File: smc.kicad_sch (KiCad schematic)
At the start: 42 parts, among them SW1 SW_Push, SW2 SW_Push, U5 W25Q128JVS, U6 RP2040, Y1 12MHz 20pF

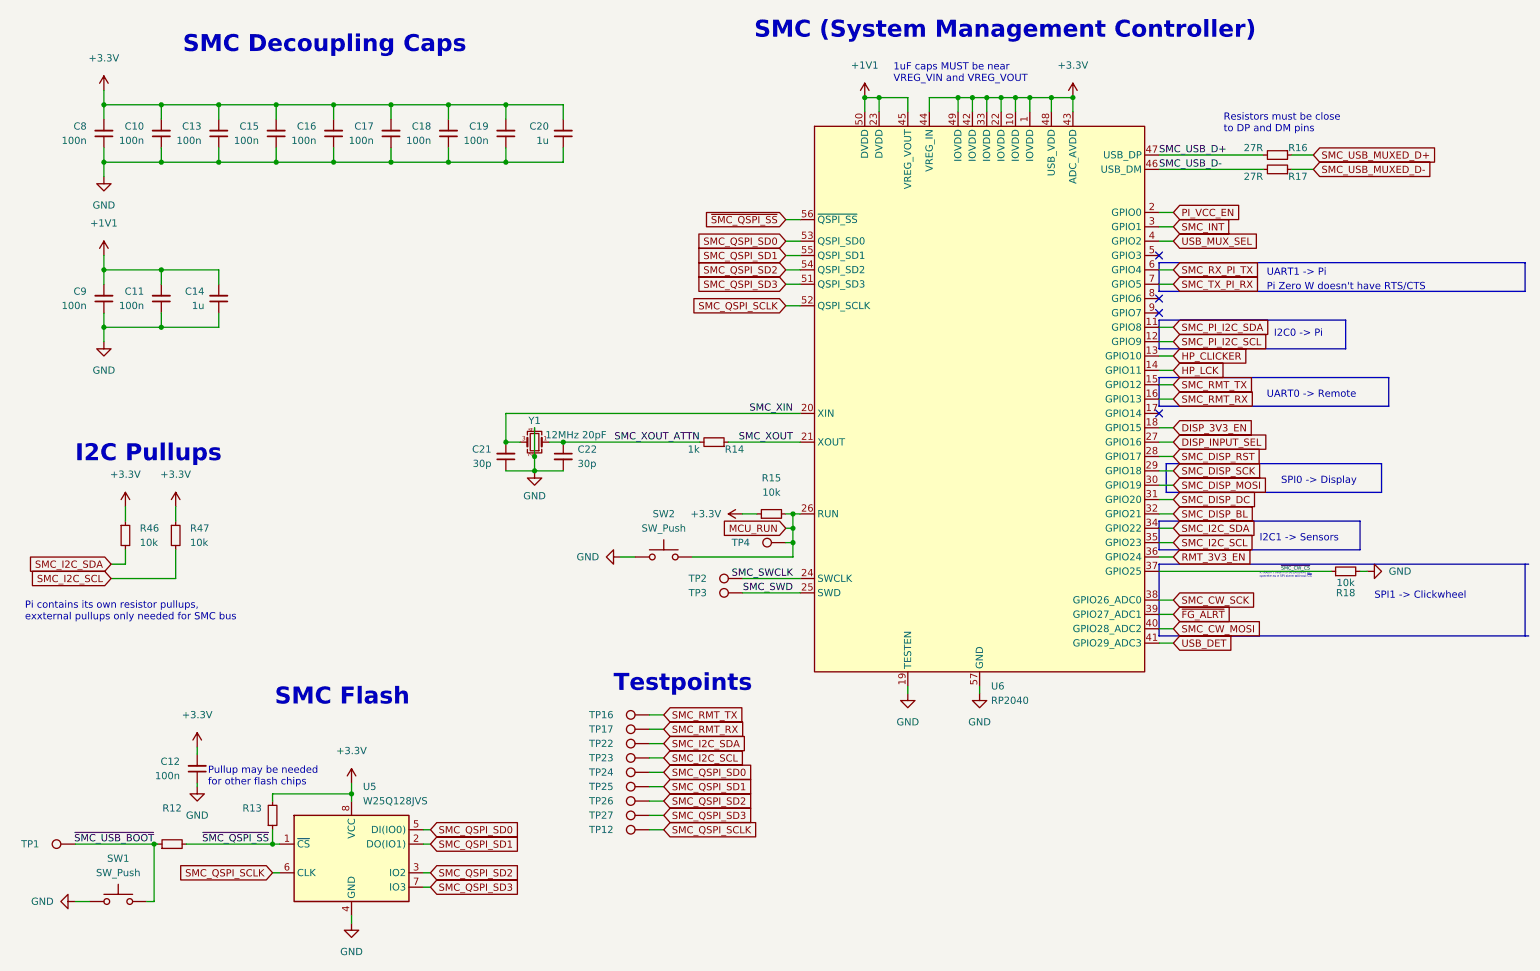
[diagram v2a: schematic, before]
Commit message: schematic: add resistors to allow latching pi power
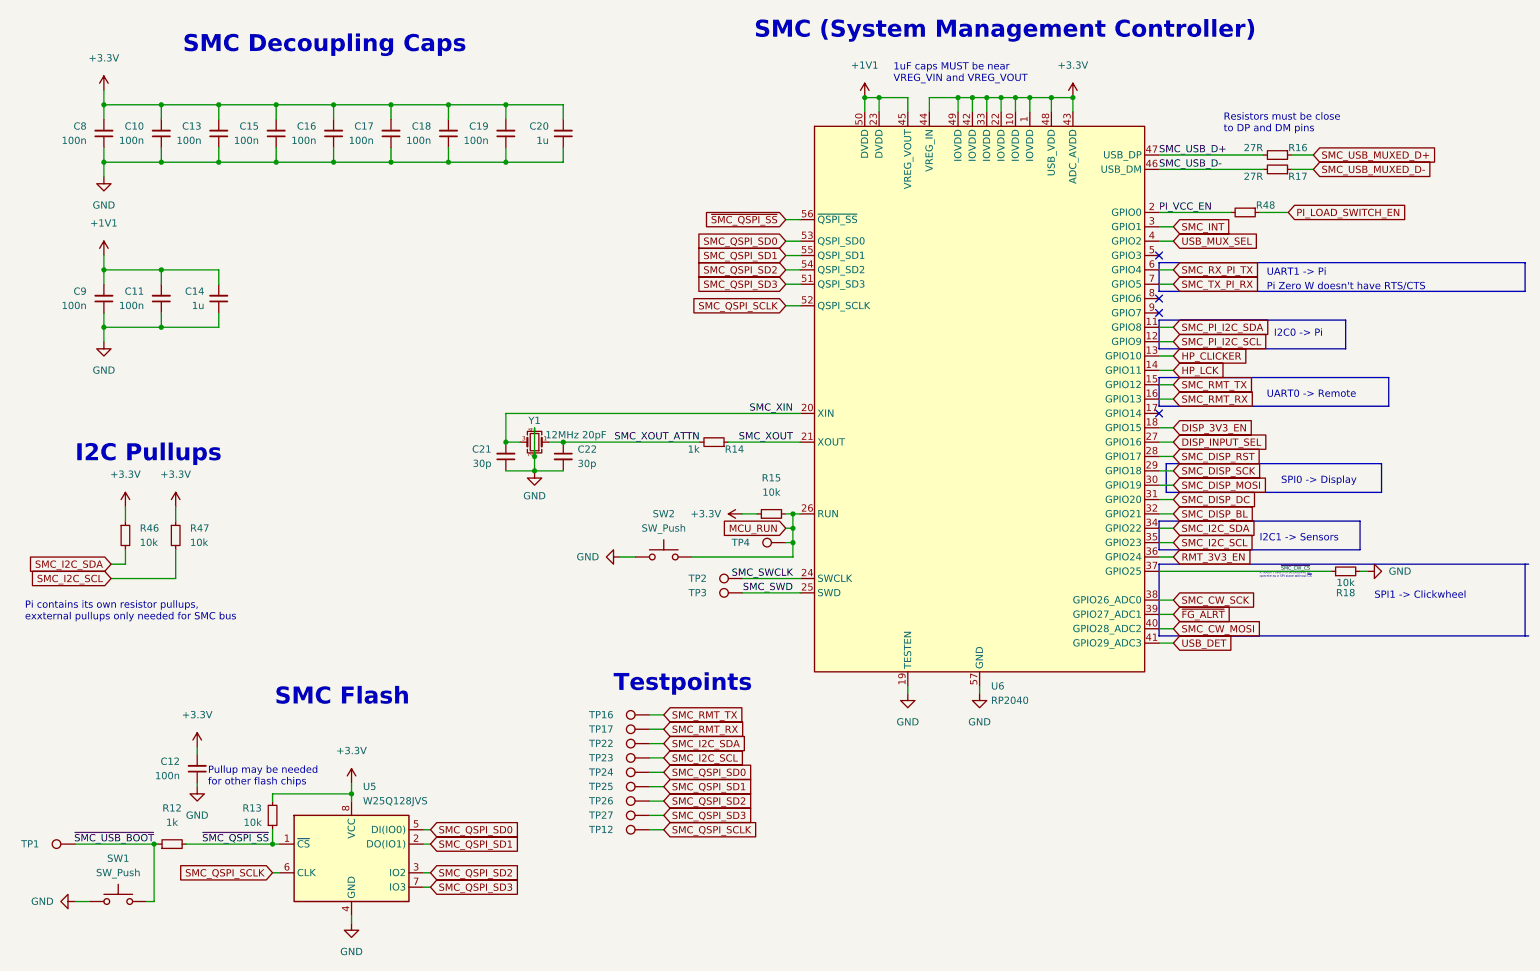
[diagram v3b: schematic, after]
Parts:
- added R48: (no value), symbol Device:R_Small
- R12: value (none) -> 1k
- R13: value (none) -> 10k
- SW1, SW2: footprint (none) -> Gigahawk:SW_Push_1P1T_NO_CK_KMR2
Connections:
- net PI_VCC_EN: now also R48.2
- new net PI_LOAD_SWITCH_EN: R48.1
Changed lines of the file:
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@@
     (stroke (width 0) (type default) (color 0 0 0 0))
   )
-  (wire (pts (xy 217.17 63.5) (xy 219.71 63.5))
+  (wire (pts (xy 217.17 63.5) (xy 229.87 63.5))
     (stroke (width 0) (type default) (color 0 0 0 0))
   )
@@
   )
   (wire (pts (xy 217.17 76.2) (xy 219.71 76.2))
+    (stroke (width 0) (type default) (color 0 0 0 0))
+  )
+  (wire (pts (xy 234.95 63.5) (xy 240.03 63.5))
     (stroke (width 0) (type default) (color 0 0 0 0))
   )
@@
   (label "~{SMC_QSPI_SS}" (at 59.69 175.26 180)
     (effects (font (size 1.27 1.27)) (justify right bottom))
+  )
+  (label "PI_VCC_EN" (at 217.17 63.5 0)
+    (effects (font (size 1.27 1.27)) (justify left bottom))
   )
   (label "~{SMC_CW_CS}" (at 238.76 127 0)
@@
     )
   )
+  (global_label "PI_LOAD_SWITCH_EN" (shape input) (at 240.03 63.5 0) (fields_autoplaced)
+    (effects (font (size 1.27 1.27)) (justify left))
+    (property "Intersheet References" "${INTERSHEET_REFS}" (id 0) (at 261.2512 63.4206 0)
+      (effects (font (size 1.27 1.27)) (justify left) hide)
+    )
+  )
   (global_label "SMC_QSPI_SD1" (shape input) (at 129.54 165.1 0) (fields_autoplaced)
     (effects (font (size 1.27 1.27)) (justify left))
@@
     )
   )
-  (global_label "PI_VCC_EN" (shape input) (at 219.71 63.5 0) (fields_autoplaced)
-    (effects (font (size 1.27 1.27)) (justify left))
-    (property "Intersheet References" "${INTERSHEET_REFS}" (id 0) (at 231.9202 63.5794 0)
-      (effects (font (size 1.27 1.27)) (justify left) hide)
-    )
-  )
   (global_label "SMC_TX_PI_RX" (shape input) (at 219.71 76.2 0) (fields_autoplaced)
     (effects (font (size 1.27 1.27)) (justify left))
@@
     (in_bom yes) (on_board yes) (fields_autoplaced)
     (property "Reference" "R12" (id 0) (at 42.545 168.91 90))
-    (property "Value" "" (id 1) (at 42.545 171.45 90))
+    (property "Value" "1k" (id 1) (at 42.545 171.45 90))
     (property "Footprint" "Resistor_SMD:R_0402_1005Metric" (id 2) (at 42.545 175.26 0)
       (effects (font (size 1.27 1.27)) hide)
@@
       (effects (font (size 1.27 1.27)) (justify right))
     )
-    (property "Value" "" (id 1) (at 58.42 171.4499 0)
+    (property "Value" "10k" (id 1) (at 58.42 171.4499 0)
       (effects (font (size 1.27 1.27)) (justify right))
     )
@@
     )
     (pin "1")
+  )
+  (symbol (lib_id "Device:R_Small") (at 232.41 63.5 270) (unit 1)
+    (in_bom yes) (on_board yes)
+    (property "Reference" "R48" (id 0) (at 234.315 62.23 90)
+      (effects (font (size 1.27 1.27)) (justify left))
+    )
+    (property "Value" "" (id 1) (at 229.87 62.23 90)
+      (effects (font (size 1.27 1.27)) (justify right))
+    )
+    (property "Footprint" "" (id 2) (at 232.41 63.5 0)
+      (effects (font (size 1.27 1.27)) hide)
+    )
+    (property "Datasheet" "~" (id 3) (at 232.41 63.5 0)
+      (effects (font (size 1.27 1.27)) hide)
+    )
+    (pin "1")
+    (pin "2")
   )
   (symbol (lib_id "Device:R_Small") (at 43.18 120.65 0) (unit 1)
@@
     (property "Reference" "SW1" (id 0) (at 33.02 177.8 0))
     (property "Value" "SW_Push" (id 1) (at 33.02 180.34 0))
-    (property "Footprint" "" (id 2) (at 33.02 180.34 0)
+    (property "Footprint" "Gigahawk:SW_Push_1P1T_NO_CK_KMR2" (id 2) (at 33.02 180.34 0)
       (effects (font (size 1.27 1.27)) hide)
     )
@@
     (property "Reference" "SW2" (id 0) (at 129.54 116.84 0))
     (property "Value" "SW_Push" (id 1) (at 129.54 119.38 0))
-    (property "Footprint" "" (id 2) (at 129.54 119.38 0)
-      (effects (font (size 1.27 1.27)) hide)
-    )
+    (property "Footprint" "Gigahawk:SW_Push_1P1T_NO_CK_KMR2" (id 2) (at 129.54 119.38 0)
+      (effects (font (size 1.27 1.27)) hide)
+    )

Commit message: compute: finish layout and routing
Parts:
- added D4: (no value), symbol Device:LED
- added R50: (no value), symbol Device:R
- added TP34: TestPoint, TestPoint:TestPoint_Pad_D1.5mm, symbol Connector:TestPoint
- R48: value (none) -> 1k; footprint (none) -> Resistor_SMD:R_0402_1005Metric
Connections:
- net GND: now also R50.2
- net SMC_RX_PI_TX: now also U6.7 (GPIO5); no longer U6.6 (GPIO4)
- net SMC_TX_PI_RX: now also U6.6 (GPIO4); no longer U6.7 (GPIO5)
- net SMC_LED: now reaches U6.5 (GPIO3)
- net SMC_LED: now also D4.2 (A), TP34.1
- new net: D4.1 (K), R50.1
- no-connect marks 4 -> 3
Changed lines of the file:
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@@
   (no_connect (at 217.17 81.28))
   (no_connect (at 217.17 78.74))
-  (no_connect (at 217.17 71.12))
   (wire (pts (xy 217.17 93.98) (xy 219.71 93.98))
     (stroke (width 0) (type default) (color 0 0 0 0))
@@
     (stroke (width 0) (type default) (color 0 0 0 0))
   )
+  (wire (pts (xy 217.17 71.12) (xy 219.71 71.12))
+    (stroke (width 0) (type default) (color 0 0 0 0))
+  )
   (wire (pts (xy 217.17 116.84) (xy 219.71 116.84))
     (stroke (width 0) (type default) (color 0 0 0 0))
@@
     (stroke (width 0) (type default) (color 0 0 0 0))
   )
+  (wire (pts (xy 127 175.26) (xy 129.54 175.26))
+    (stroke (width 0) (type default) (color 0 0 0 0))
+  )
   (polyline (pts (xy 217.17 82.55) (xy 250.19 82.55))
     (stroke (width 0) (type default) (color 0 0 0 0))
@@
     (stroke (width 0) (type default) (color 0 0 0 0))
   )
+  (wire (pts (xy 119.38 74.93) (xy 119.38 77.47))
+    (stroke (width 0) (type default) (color 0 0 0 0))
+  )
   (wire (pts (xy 121.92 124.46) (xy 124.46 124.46))
     (stroke (width 0) (type default) (color 0 0 0 0))
@@
     (stroke (width 0) (type default) (color 0 0 0 0))
   )
+  (wire (pts (xy 119.38 64.77) (xy 119.38 67.31))
+    (stroke (width 0) (type default) (color 0 0 0 0))
+  )
   (wire (pts (xy 134.62 124.46) (xy 152.4 124.46))
     (stroke (width 0) (type default) (color 0 0 0 0))
@@
   )
   (wire (pts (xy 186.69 43.18) (xy 186.69 45.72))
+    (stroke (width 0) (type default) (color 0 0 0 0))
+  )
+  (wire (pts (xy 119.38 85.09) (xy 119.38 87.63))
     (stroke (width 0) (type default) (color 0 0 0 0))
   )
@@
     )
   )
+  (global_label "SMC_LED" (shape input) (at 129.54 175.26 0) (fields_autoplaced)
+    (effects (font (size 1.27 1.27)) (justify left))
+    (property "Intersheet References" "${INTERSHEET_REFS}" (id 0) (at 140.2988 175.1806 0)
+      (effects (font (size 1.27 1.27)) (justify left) hide)
+    )
+  )
   (global_label "~{FG_ALRT}" (shape input) (at 219.71 134.62 0) (fields_autoplaced)
     (effects (font (size 1.27 1.27)) (justify left))
@@
     )
   )
+  (global_label "SMC_LED" (shape input) (at 119.38 64.77 0) (fields_autoplaced)
+    (effects (font (size 1.27 1.27)) (justify left))
+    (property "Intersheet References" "${INTERSHEET_REFS}" (id 0) (at 130.1388 64.6906 0)
+      (effects (font (size 1.27 1.27)) (justify left) hide)
+    )
+  )
   (global_label "SMC_QSPI_SD2" (shape input) (at 129.54 167.64 0) (fields_autoplaced)
     (effects (font (size 1.27 1.27)) (justify left))
@@
     )
   )
+  (global_label "SMC_LED" (shape input) (at 219.71 71.12 0) (fields_autoplaced)
+    (effects (font (size 1.27 1.27)) (justify left))
+    (property "Intersheet References" "${INTERSHEET_REFS}" (id 0) (at 230.4688 71.0406 0)
+      (effects (font (size 1.27 1.27)) (justify left) hide)
+    )
+  )
   (global_label "HP_CLICKER" (shape input) (at 219.71 88.9 0) (fields_autoplaced)
     (effects (font (size 1.27 1.27)) (justify left))
@@
     )
   )
-  (global_label "SMC_RX_PI_TX" (shape input) (at 219.71 73.66 0) (fields_autoplaced)
-    (effects (font (size 1.27 1.27)) (justify left))
-    (property "Intersheet References" "${INTERSHEET_REFS}" (id 0) (at 235.4883 73.5806 0)
+  (global_label "SMC_RX_PI_TX" (shape input) (at 219.71 76.2 0) (fields_autoplaced)
+    (effects (font (size 1.27 1.27)) (justify left))
+    (property "Intersheet References" "${INTERSHEET_REFS}" (id 0) (at 235.4883 76.1206 0)
       (effects (font (size 1.27 1.27)) (justify left) hide)
     )
@@
     )
   )
-  (global_label "SMC_TX_PI_RX" (shape input) (at 219.71 76.2 0) (fields_autoplaced)
-    (effects (font (size 1.27 1.27)) (justify left))
-    (property "Intersheet References" "${INTERSHEET_REFS}" (id 0) (at 235.4883 76.1206 0)
+  (global_label "SMC_TX_PI_RX" (shape input) (at 219.71 73.66 0) (fields_autoplaced)
+    (effects (font (size 1.27 1.27)) (justify left))
+    (property "Intersheet References" "${INTERSHEET_REFS}" (id 0) (at 235.4883 73.5806 0)
       (effects (font (size 1.27 1.27)) (justify left) hide)
     )
@@
     (pin "2")
   )
+  (symbol (lib_id "Device:LED") (at 119.38 71.12 90) (unit 1)
+    (in_bom yes) (on_board yes) (fields_autoplaced)
+    (property "Reference" "D4" (id 0) (at 123.19 71.4374 90)
+      (effects (font (size 1.27 1.27)) (justify right))
+    )
+    (property "Value" "" (id 1) (at 123.19 73.9774 90)
+      (effects (font (size 1.27 1.27)) (justify right))
+    )
+    (property "Footprint" "" (id 2) (at 119.38 71.12 0)
+      (effects (font (size 1.27 1.27)) hide)
+    )
+    (property "Datasheet" "~" (id 3) (at 119.38 71.12 0)
+      (effects (font (size 1.27 1.27)) hide)
+    )
+    (pin "1")
+    (pin "2")
+  )
   (symbol (lib_id "power:+1V1") (at 165.1 43.18 0) (unit 1)
     (in_bom yes) (on_board yes) (fields_autoplaced)
@@
       (effects (font (size 1.27 1.27)) (justify left))
     )
-    (property "Value" "" (id 1) (at 229.87 62.23 90)
-      (effects (font (size 1.27 1.27)) (justify right))
-    )
-    (property "Footprint" "" (id 2) (at 232.41 63.5 0)
+    (property "Value" "1k" (id 1) (at 229.87 62.23 90)
+      (effects (font (size 1.27 1.27)) (justify right))
+    )
+    (property "Footprint" "Resistor_SMD:R_0402_1005Metric" (id 2) (at 232.41 63.5 0)
       (effects (font (size 1.27 1.27)) hide)
     )
@@
     (pin "1")
     (pin "2")
+  )
+  (symbol (lib_id "power:GND") (at 119.38 87.63 0) (unit 1)
+    (in_bom yes) (on_board yes) (fields_autoplaced)
+    (property "Reference" "#PWR0144" (id 0) (at 119.38 93.98 0)
+      (effects (font (size 1.27 1.27)) hide)
+    )
+    (property "Value" "" (id 1) (at 119.38 92.71 0))
+    (property "Footprint" "" (id 2) (at 119.38 87.63 0)
+      (effects (font (size 1.27 1.27)) hide)
+    )
+    (property "Datasheet" "" (id 3) (at 119.38 87.63 0)
+      (effects (font (size 1.27 1.27)) hide)
+    )
+    (pin "1")
   )
   (symbol (lib_id "Device:R_Small") (at 43.18 120.65 0) (unit 1)
@@
     (pin "1")
     (pin "2")
+  )
+  (symbol (lib_id "Connector:TestPoint") (at 127 175.26 90) (unit 1)
+    (in_bom yes) (on_board yes)
+    (property "Reference" "TP34" (id 0) (at 120.65 175.26 90)
+      (effects (font (size 1.27 1.27)) (justify left))
+    )
+    (property "Value" "TestPoint" (id 1) (at 124.9679 172.72 0)
+      (effects (font (size 1.27 1.27)) (justify left) hide)
+    )
+    (property "Footprint" "TestPoint:TestPoint_Pad_D1.5mm" (id 2) (at 127 170.18 0)
+      (effects (font (size 1.27 1.27)) hide)
+    )
+    (property "Datasheet" "~" (id 3) (at 127 170.18 0)
+      (effects (font (size 1.27 1.27)) hide)
+    )
+    (pin "1")
   )
   (symbol (lib_id "Device:C_Small") (at 50.8 49.53 0) (mirror x) (unit 1)
@@
     (pin "9")
   )
+  (symbol (lib_id "Device:R") (at 119.38 81.28 0) (unit 1)
+    (in_bom yes) (on_board yes) (fields_autoplaced)
+    (property "Reference" "R50" (id 0) (at 121.92 80.0099 0)
+      (effects (font (size 1.27 1.27)) (justify left))
+    )
+    (property "Value" "" (id 1) (at 121.92 82.5499 0)
+      (effects (font (size 1.27 1.27)) (justify left))
+    )
+    (property "Footprint" "" (id 2) (at 117.602 81.28 90)
+      (effects (font (size 1.27 1.27)) hide)
+    )
+    (property "Datasheet" "~" (id 3) (at 119.38 81.28 0)
+      (effects (font (size 1.27 1.27)) hide)
+    )
+    (pin "1")
+    (pin "2")
+  )
   (symbol (lib_id "power:GND") (at 121.92 124.46 270) (unit 1)

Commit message: ci: prepare files for CI
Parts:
- D4: value (none) -> GRN; footprint (none) -> LED_SMD:LED_0402_1005Metric
- R50: value (none) -> 470R; footprint (none) -> Resistor_SMD:R_0402_1005Metric
- U5: footprint Package_SON:WSON-8-1EP_6x5mm_P1.27mm_EP3.4x4.3mm -> Gigahawk:WSON-8-1EP_6x5mm_P1.27mm_EP3.4x4.3mm
- Y1: footprint Crystal:Crystal_SMD_2520-4Pin_2.5x2.0mm -> Gigahawk:Crystal_SMD_2520-4Pin_2.5x2.0mm
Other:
- title: (none) -> piPod IO/SMC Board
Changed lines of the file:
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@@
 (kicad_sch (version 20211123) (generator eeschema)
   (paper "A4")
+  (title_block
+    (title "piPod IO/SMC Board")
+    (date "${DATE}")
+    (rev "%{TAG} (${REVISION})")
+  )
   (junction (at 198.12 43.18) (diameter 0) (color 0 0 0 0)
   )
@@
       (effects (font (size 1.27 1.27)) (justify right))
     )
-    (property "Value" "" (id 1) (at 123.19 73.9774 90)
-      (effects (font (size 1.27 1.27)) (justify right))
-    )
-    (property "Footprint" "" (id 2) (at 119.38 71.12 0)
+    (property "Value" "GRN" (id 1) (at 123.19 73.9774 90)
+      (effects (font (size 1.27 1.27)) (justify right))
+    )
+    (property "Footprint" "LED_SMD:LED_0402_1005Metric" (id 2) (at 119.38 71.12 0)
       (effects (font (size 1.27 1.27)) hide)
     )
@@
       (effects (font (size 1.27 1.27)) hide)
     )
-    (property "Value" "" (id 1) (at 119.38 92.71 0))
+    (property "Value" "GND" (id 1) (at 119.38 92.71 0))
     (property "Footprint" "" (id 2) (at 119.38 87.63 0)
       (effects (font (size 1.27 1.27)) hide)
@@
       (effects (font (size 1.27 1.27)) (justify left))
     )
-    (property "Footprint" "Package_SON:WSON-8-1EP_6x5mm_P1.27mm_EP3.4x4.3mm" (id 2) (at 74.295 177.8 0)
+    (property "Footprint" "Gigahawk:WSON-8-1EP_6x5mm_P1.27mm_EP3.4x4.3mm" (id 2) (at 74.295 177.8 0)
       (effects (font (size 1.27 1.27)) hide)
     )
@@
       (effects (font (size 1.27 1.27)) (justify right))
     )
-    (property "Footprint" "Crystal:Crystal_SMD_2520-4Pin_2.5x2.0mm" (id 2) (at 106.68 104.14 0)
+    (property "Footprint" "Gigahawk:Crystal_SMD_2520-4Pin_2.5x2.0mm" (id 2) (at 106.68 104.14 0)
       (effects (font (size 1.27 1.27)) hide)
     )
@@
       (effects (font (size 1.27 1.27)) (justify left))
     )
-    (property "Value" "" (id 1) (at 121.92 82.5499 0)
-      (effects (font (size 1.27 1.27)) (justify left))
-    )
-    (property "Footprint" "" (id 2) (at 117.602 81.28 90)
-      (effects (font (size 1.27 1.27)) hide)
-    )
+    (property "Value" "470R" (id 1) (at 121.92 82.5499 0)
+      (effects (font (size 1.27 1.27)) (justify left))
+    )
+    (property "Footprint" "Resistor_SMD:R_0402_1005Metric" (id 2) (at 117.602 81.28 90)
+      (effects (font (size 1.27 1.27)) hide)
+    )

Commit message: ci: add vendor/distributor part numbers to bom
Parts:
- U6: Mouser Part RPI Chip RP2040-7-500 -> RPI Chip RP2040-7-500
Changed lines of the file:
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@@
       (effects (font (size 1.27 1.27)) hide)
     )
-    (property "Mouser Part" "RPI Chip RP2040-7-500 " (id 10) (at 185.42 99.06 0)
+    (property "Mouser Part" "RPI Chip RP2040-7-500" (id 10) (at 185.42 99.06 0)
       (effects (font (size 1.27 1.27)) hide)
     )
